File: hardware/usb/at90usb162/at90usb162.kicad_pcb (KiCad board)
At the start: 2 copper layers, 47.5 x 44.9 mm, 24 parts, among them IC1 AT90USB162-A, J1 USERPORT, P1 USB, P2 RESET, X1 8Mhz

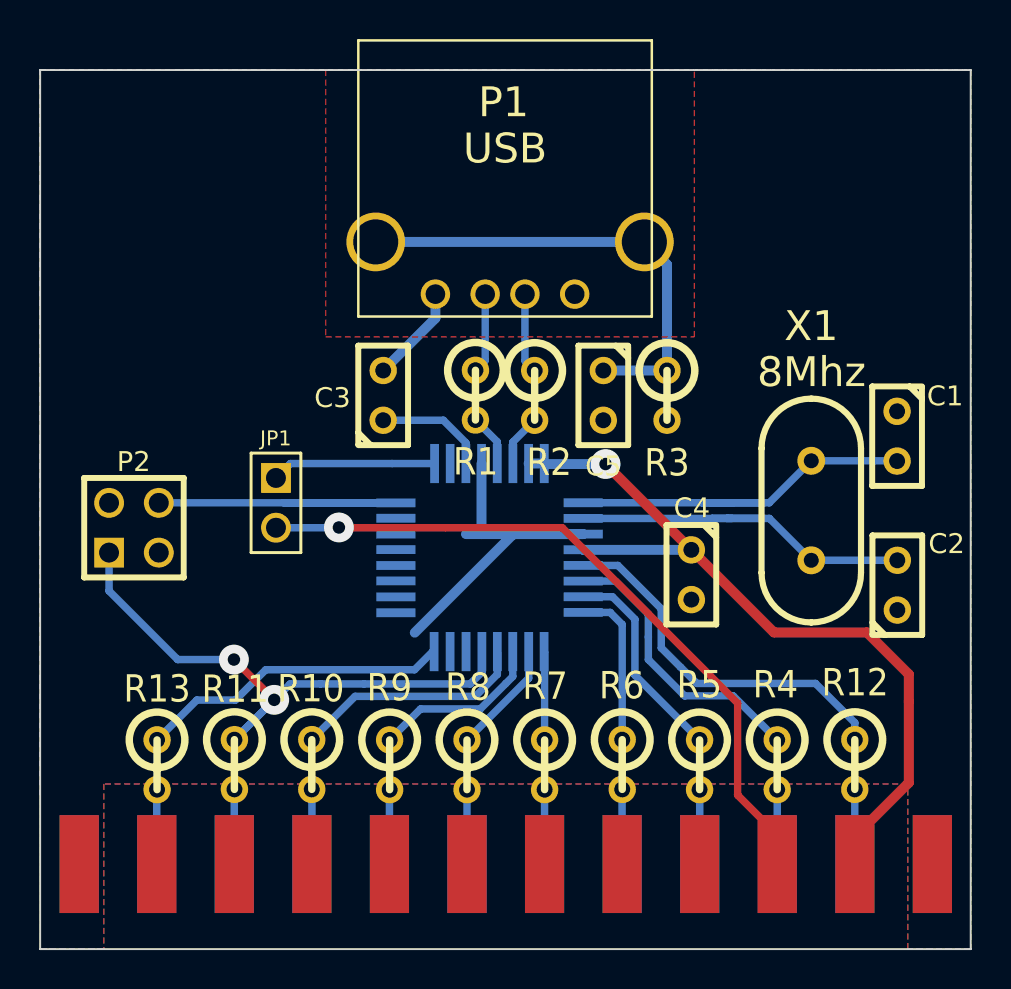
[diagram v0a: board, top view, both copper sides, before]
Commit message: Hardware: Included component values in placement sheet
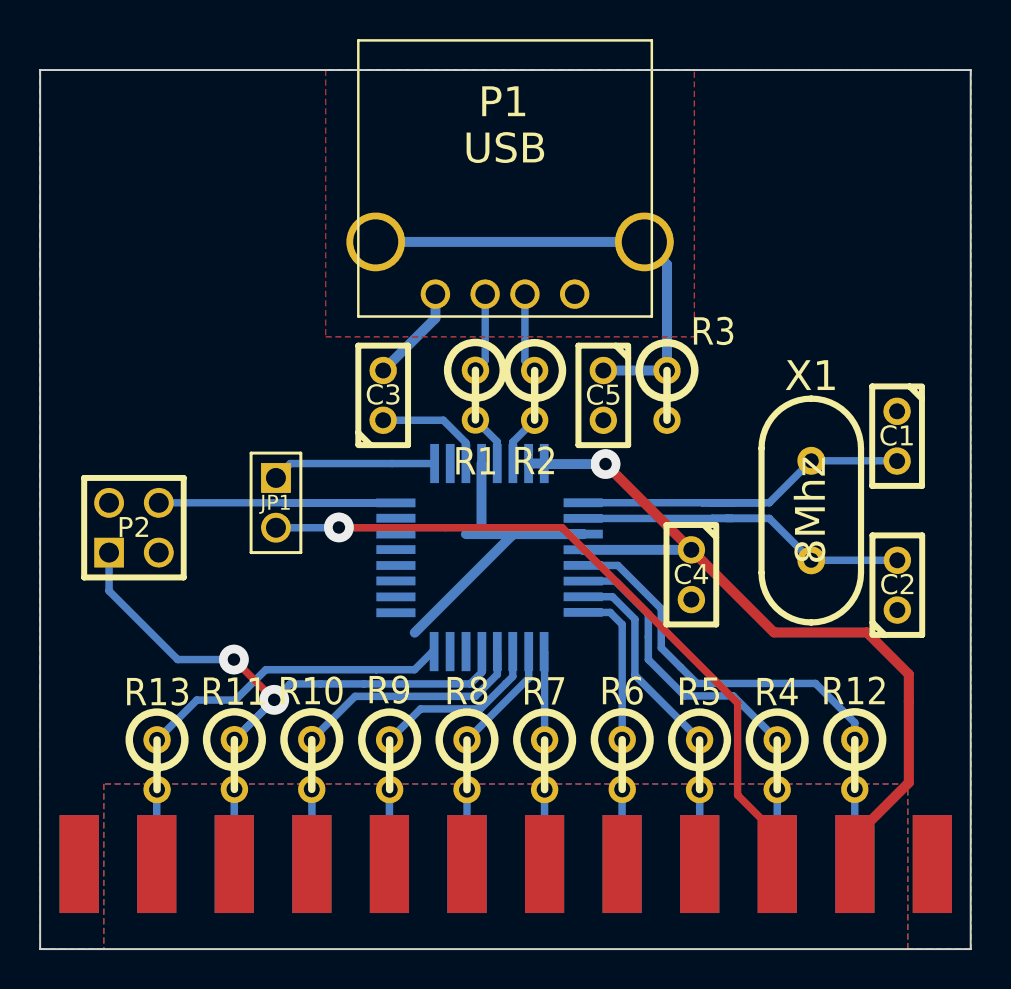
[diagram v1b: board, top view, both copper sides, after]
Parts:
- ?: renamed from J1; value USERPORT -> (none)
- JP1: value JUMPER -> (none)
- P2: value RESET -> (none)

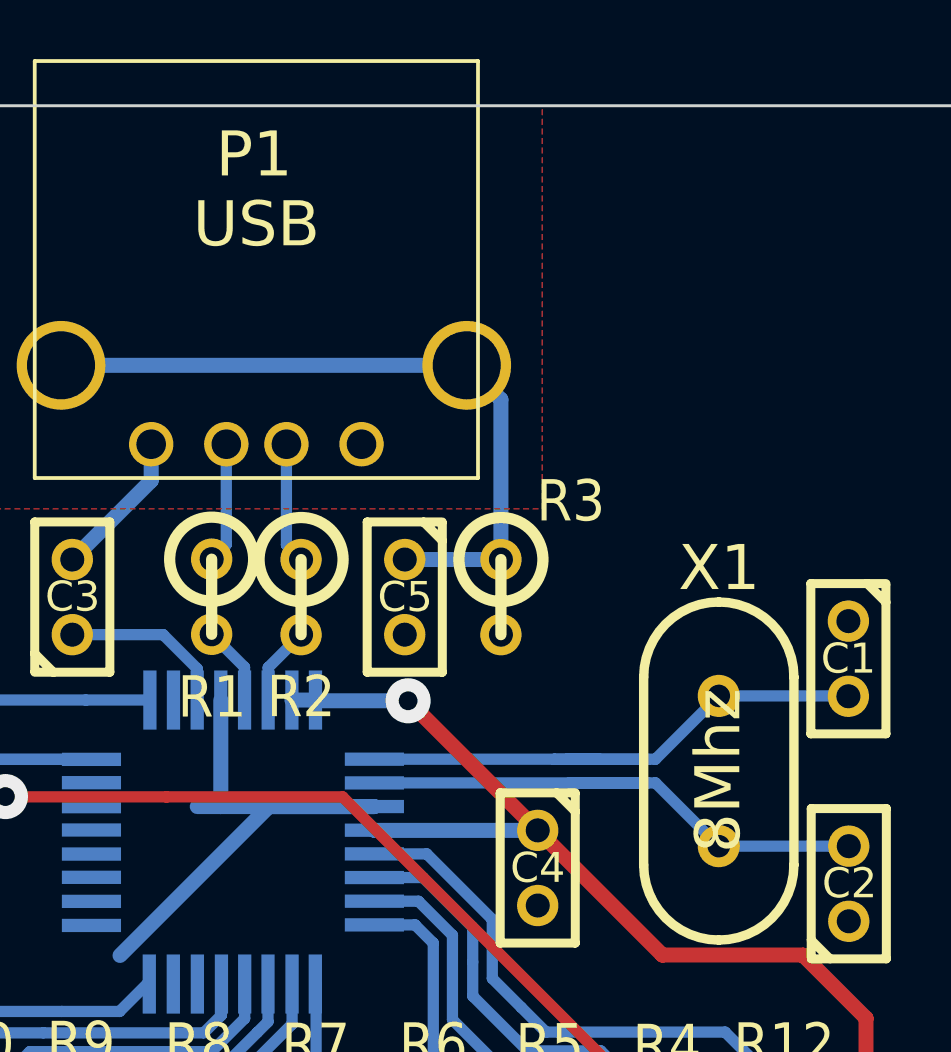
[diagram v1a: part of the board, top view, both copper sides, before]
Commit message: Fixed missing solder mask on userport connector pads
In newer versions of KiCAD the solder mask on connector pads seems to have
gone missing, resulting in non-connective connector pads.

Reported by Jon Lorusso
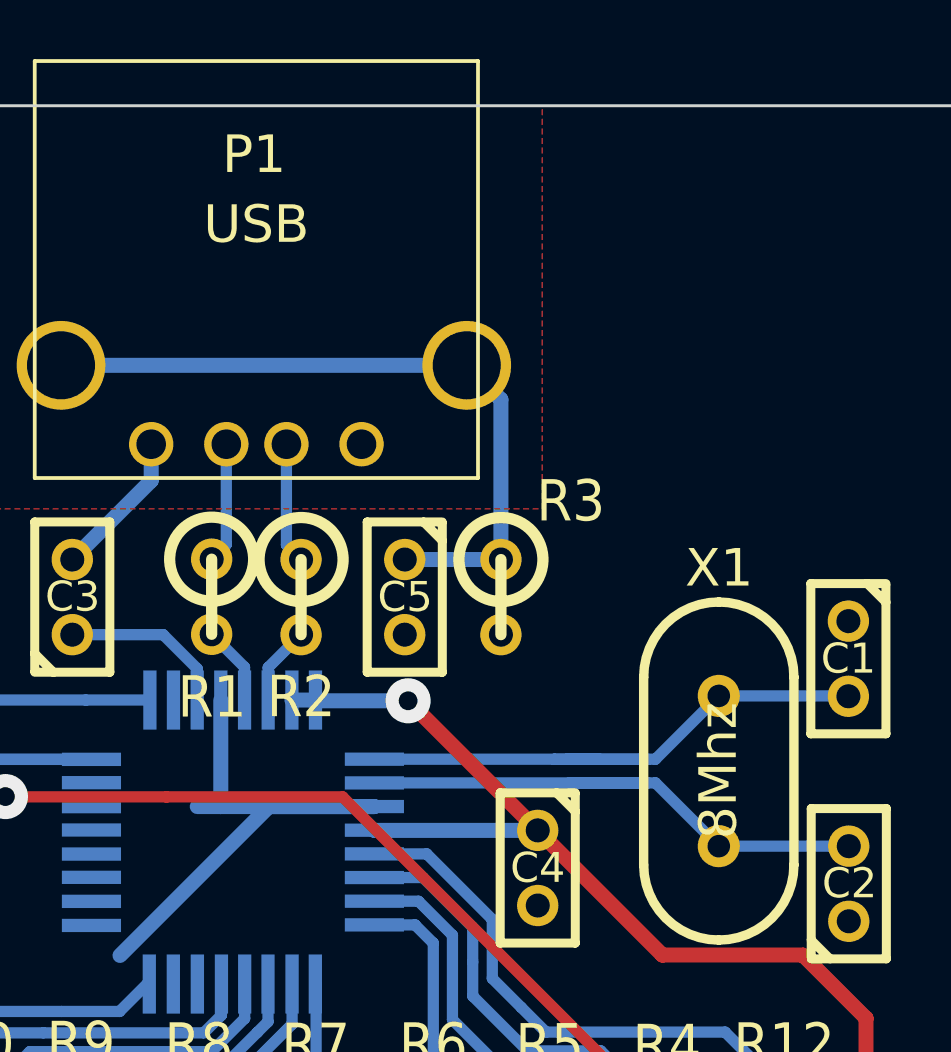
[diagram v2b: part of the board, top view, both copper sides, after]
